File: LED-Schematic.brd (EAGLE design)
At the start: 160 x 100 mm, 8 parts, among them Q1 INFINEON_IRLB8721PBFINFINEON_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, Q2 INFINEON_IRLB8721PBFINFINEON_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, Q3 INFINEON_IRLB8721PBFINFINEON_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, X1 DG3XX-03-3.5, X2 DG3XX-03-3.5, X3 DG3XX-03-3.5, X4 DG3XX-03-3.5

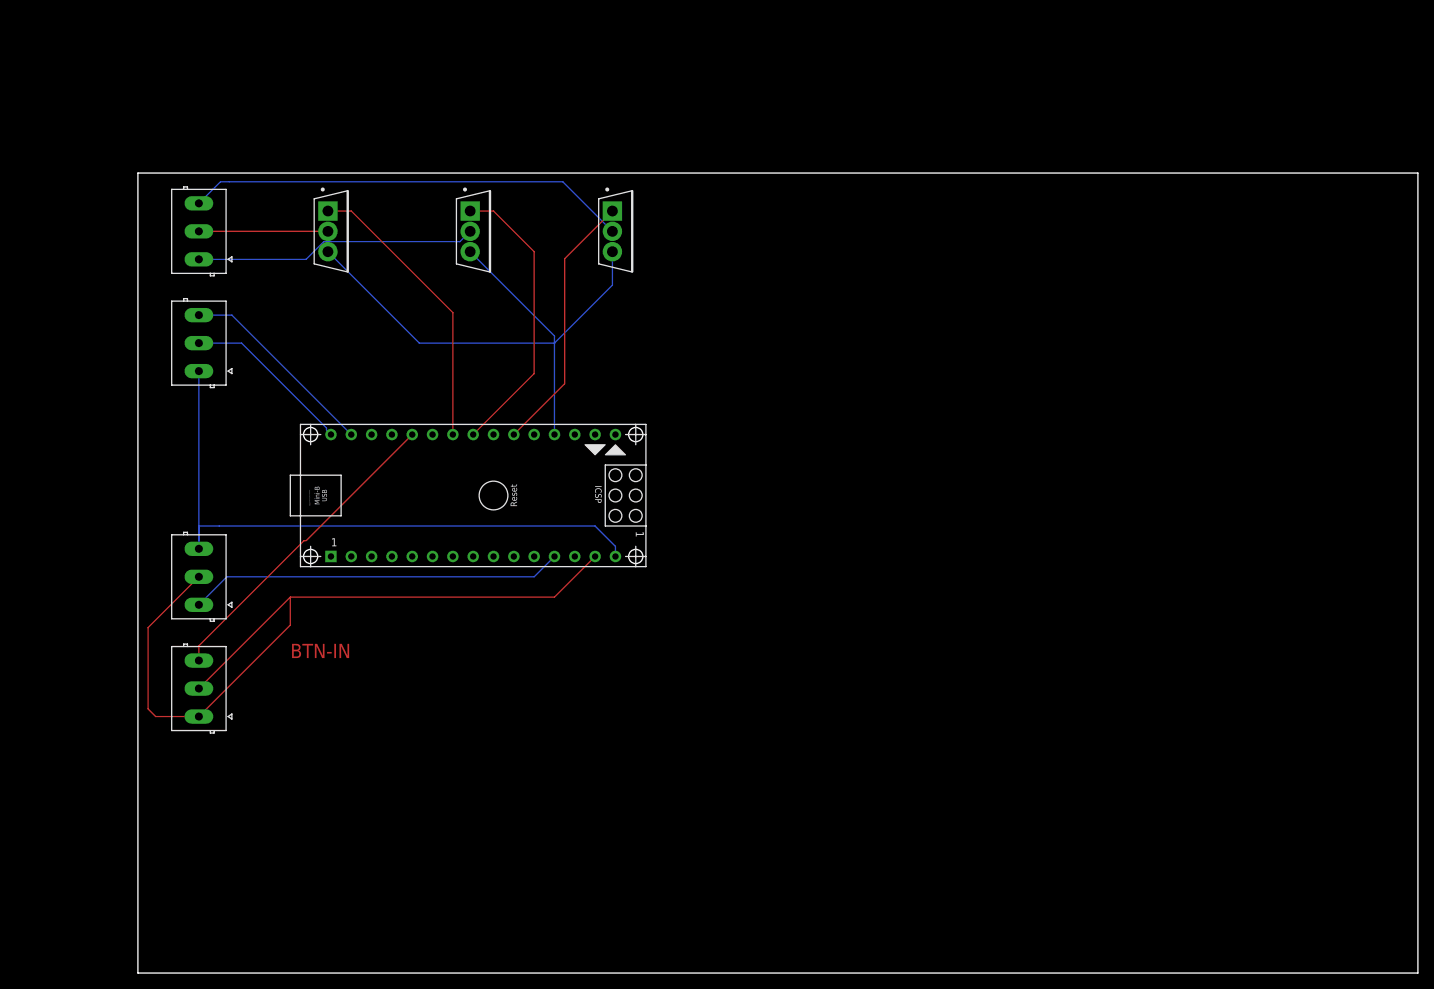
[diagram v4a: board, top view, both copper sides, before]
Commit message: addign silk screen labels
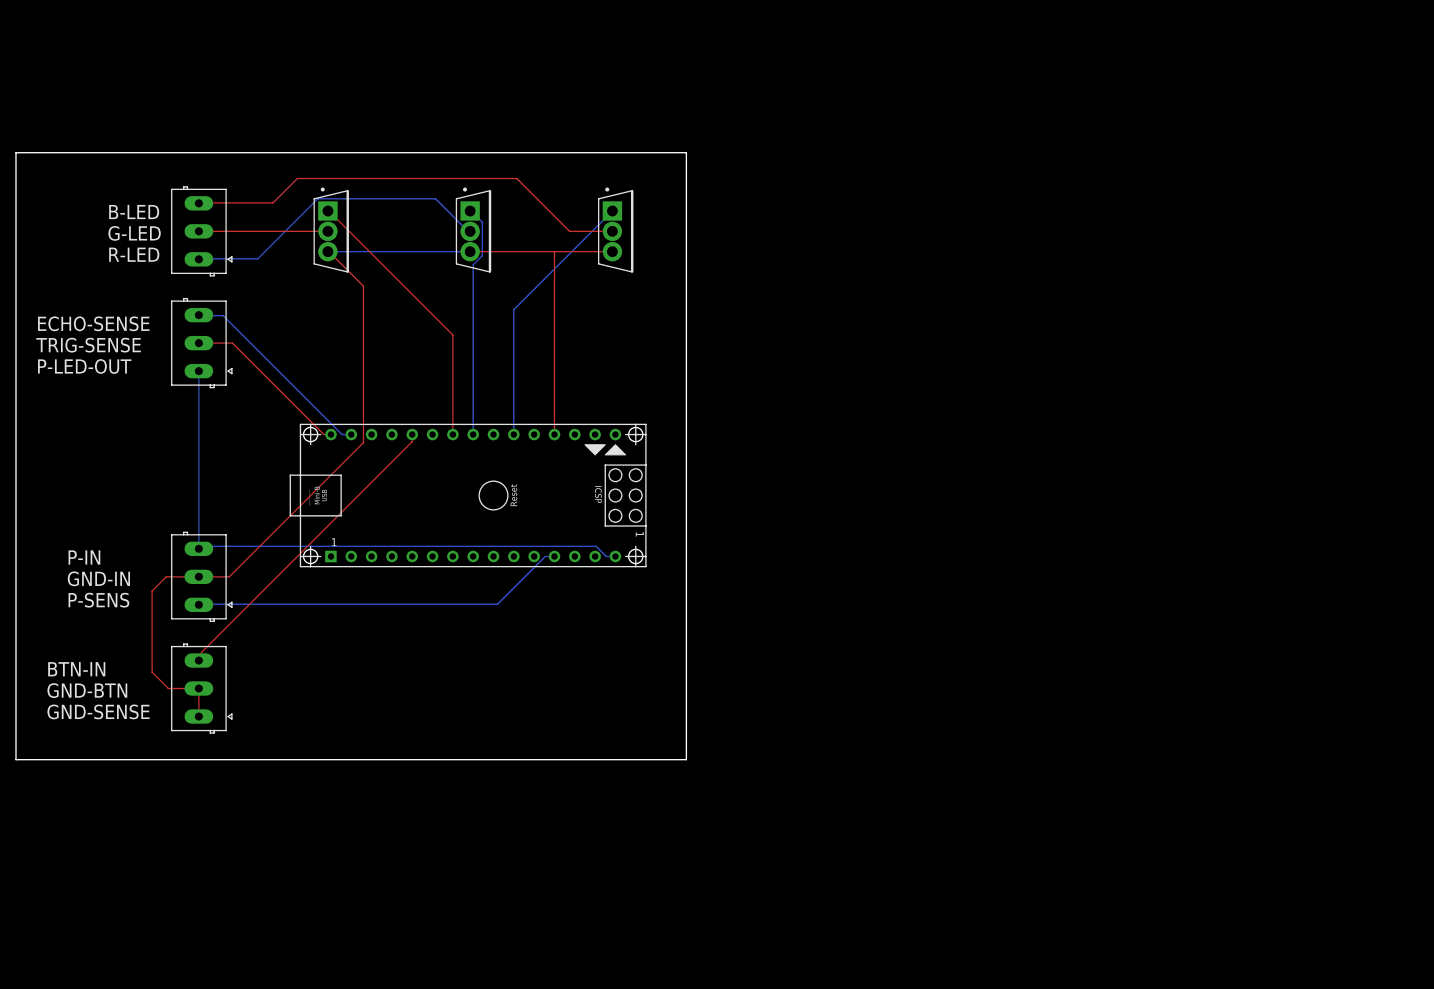
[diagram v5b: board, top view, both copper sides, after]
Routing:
- net GND: track 176.6 -> 138.6 mm
- net R-GATE: track 36.1 -> 29.1 mm
- net P-LED: track 79.6 -> 75.6 mm
- net R-LED: track 35.4 -> 38.8 mm
- net G-GATE: track 36.1 -> 34.5 mm
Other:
- board size 160 x 100 mm -> 83.8 x 75.9 mm
- board text added: "B-LED G-LED R-LED"
- board text added: "BTN-IN GND-BTN GND-SENSE"
- board text added: "ECHO-SENSE TRIG-SENSE P-LED-OUT"
- board text added: "P-IN GND-IN P-SENS"
- board text removed: "BTN-IN"

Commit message: Last Revamp, i promise
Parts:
- moved Q1 2.54 mm to (44.5, 92.7), turned to 270 degrees
- moved Q2 2.54 mm to (26.7, 92.7), turned to 270 degrees
- moved X2 2.54 mm to (7.62, 76.2), turned to 270 degrees
- moved Q3 1.27 mm to (61.0, 92.7), turned to 270 degrees
- turned X1 to 270 degrees
- turned X3 to 270 degrees
- turned X4 to 270 degrees
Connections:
- net P-LED renamed 12V
- net P-SENSE renamed 5V
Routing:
- net BTN-IN: track 39.3 -> 64.9 mm
- net 12V: track 75.6 -> 94.1 mm
- net GND: track 138.6 -> 148.1 mm
- net G-LED: track 16.1 -> 21.3 mm
- net G-GATE: track 34.5 -> 30.0 mm
- net ECHO-SENSE: track 25.3 -> 21.3 mm
- net B-LED: track 55.7 -> 58.8 mm
- net R-GATE: track 29.1 -> 27.9 mm
- net TRIG-SENSE: track 21.2 -> 20.2 mm
- net 5V: track 47.0 -> 48.0 mm
- net R-LED: track 38.8 -> 38.1 mm
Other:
- board size 83.8 x 75.9 mm -> 80 x 75.9 mm
- board text added: "IN-GND BTN-GND BTN-IN"
- board text added: "LED-12v TRIG-SENSE ECHO-SENE"
- board text added: "Made in Space By Aliens"
- board text added: "R-LED G-LED B-LED"
- board text added: "SENSE-5V SENSE-GND IN-12V"
- board text added: "Why are you reverse-engineering me? I'm Open-Source github.com/MPult"
- board text removed: "B-LED G-LED R-LED"
- board text removed: "BTN-IN GND-BTN GND-SENSE"
- board text removed: "ECHO-SENSE TRIG-SENSE P-LED-OUT"
- board text removed: "P-IN GND-IN P-SENS"

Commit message: Final Edits before production
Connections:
- new net 3.3V: ARDUINO_NANO1.2, X4.2
- net GND: no longer X4.2
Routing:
- net 3.3V: track 0.00 -> 47.4 mm
- net GND: track 148.1 -> 178.5 mm
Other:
- board text added: "IN-GND BTN-3.3V BTN-IN"
- board text added: "JLCJLCJLCJLC"
- board text removed: "IN-GND BTN-GND BTN-IN"
